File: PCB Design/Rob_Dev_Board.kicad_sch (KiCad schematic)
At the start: 0 parts

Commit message: Added component files for ESP32 and DRV8245H motor driver
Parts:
- added IC1: DRV8245HQPWPRQ1, SOP65P640X120-29N, symbol DRV8245H-Q1:DRV8245HQPWPRQ1
- added U1: ESP32-S3-WROOM-1U-N8R8, ESP32-S3-WROOM-1U-N8R8:XCVR_ESP32-S3-WROOM-1U-N8R8, symbol ESP32-S3-WROOM-1U-N8R8:ESP32-S3-WROOM-1U-N8R8
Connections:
- new net: U1.1 (GND), U1.40 (GND), U1.41_1 (GND), U1.41_2 (GND), U1.41_3 (GND), U1.41_4 (GND), U1.41_5 (GND), U1.41_6 (GND), U1.41_7 (GND), U1.41_8 (GND), U1.41_9 (GND)

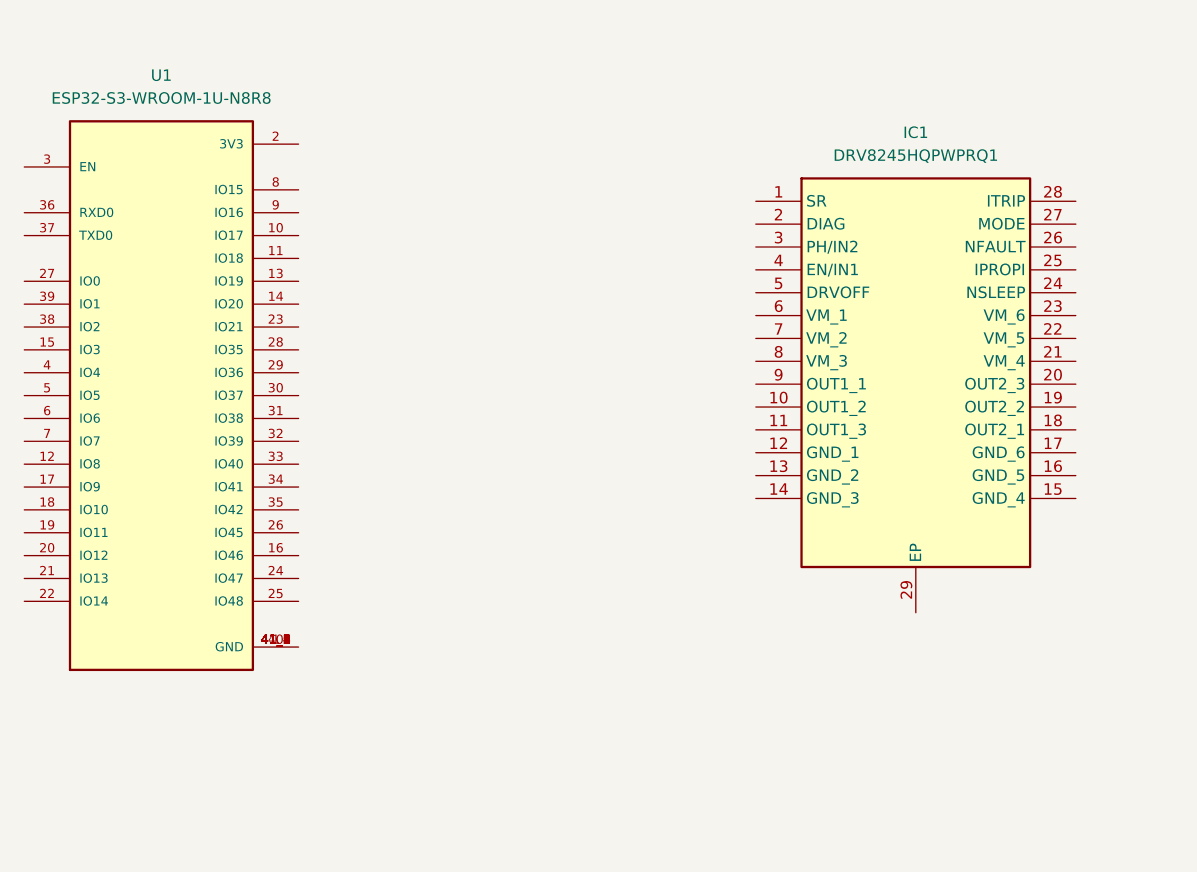
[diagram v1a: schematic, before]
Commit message: Changed components for ESP32 and motor driver to in stock options from supplier
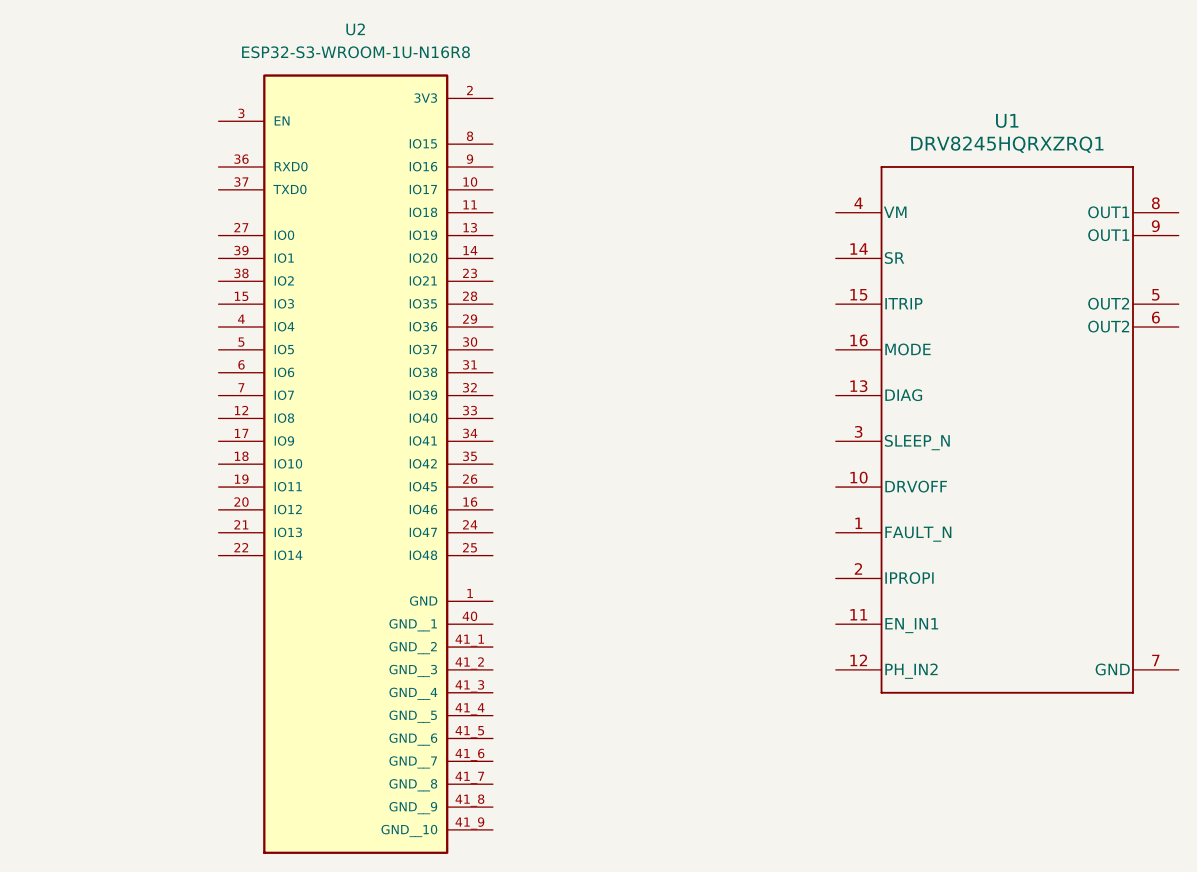
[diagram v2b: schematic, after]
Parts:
- removed IC1: DRV8245HQPWPRQ1, SOP65P640X120-29N, symbol DRV8245H-Q1:DRV8245HQPWPRQ1
- removed U1: ESP32-S3-WROOM-1U-N8R8, ESP32-S3-WROOM-1U-N8R8:XCVR_ESP32-S3-WROOM-1U-N8R8, symbol ESP32-S3-WROOM-1U-N8R8:ESP32-S3-WROOM-1U-N8R8
- added U1: DRV8245HQRXZRQ1, DRV8245H-Q1:RXZ0016A-MFG, symbol DRV8245H-Q1:DRV8245HQRXZRQ1
- added U2: ESP32-S3-WROOM-1U-N16R8, ESP32-S3-WROOM-N16R8:XCVR_ESP32-S3-WROOM-1U-N16R8, symbol ESP32-S3-WROOM-1U-N16R8:ESP32-S3-WROOM-1U-N16R8

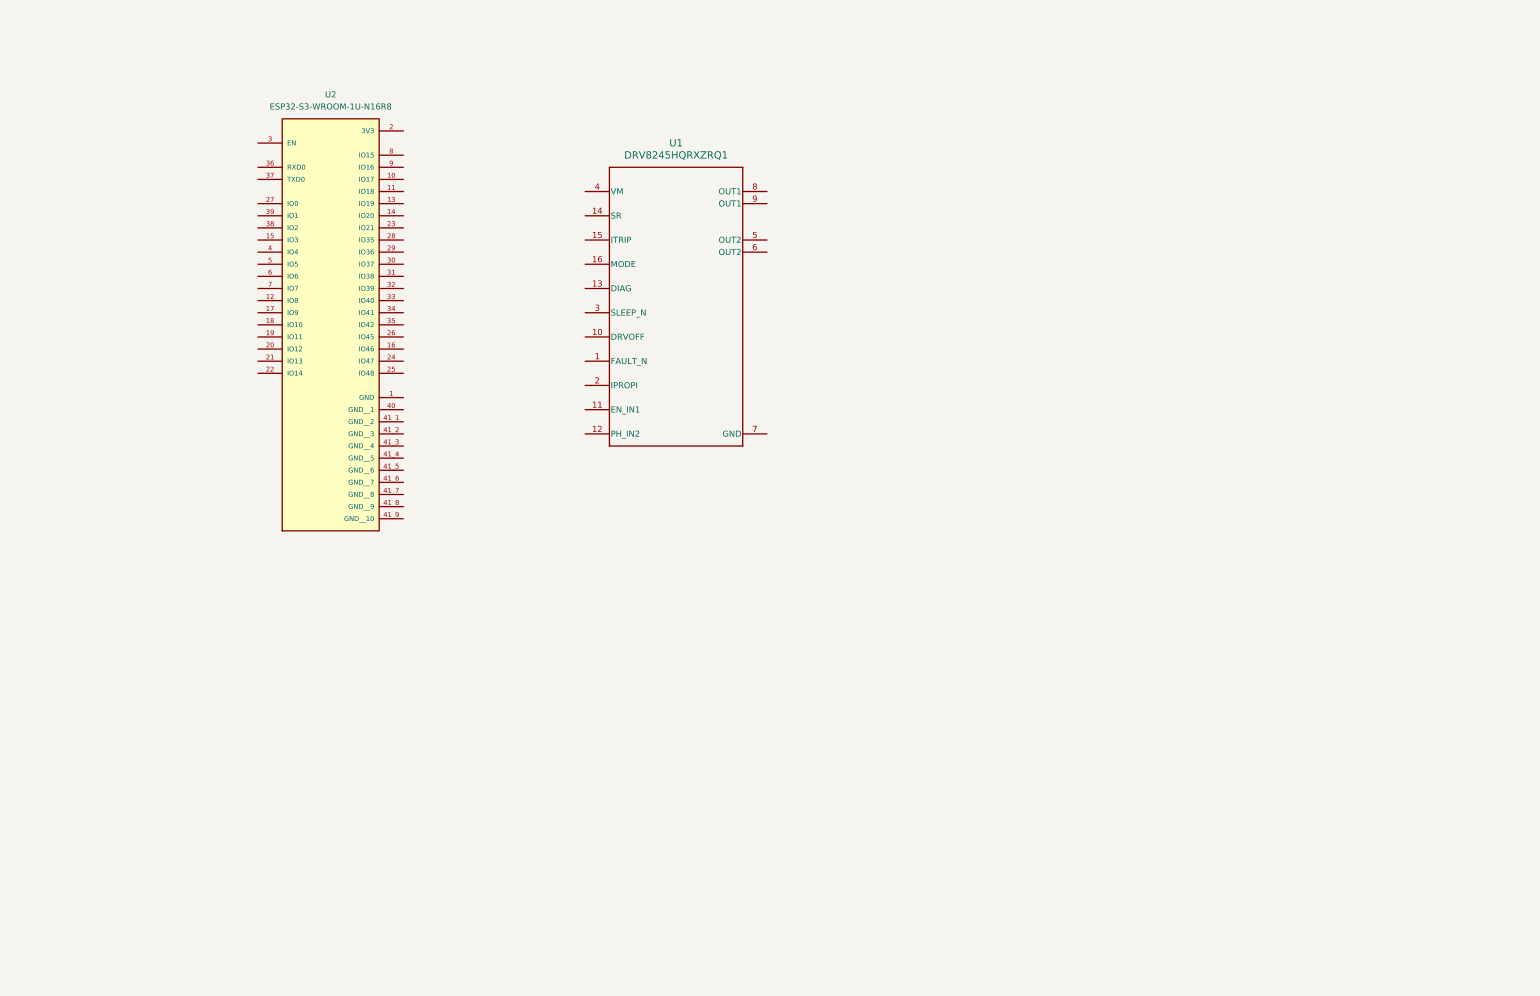
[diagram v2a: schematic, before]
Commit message: Added some more components to PCB design, added datasheet for possible BLDC motor driver
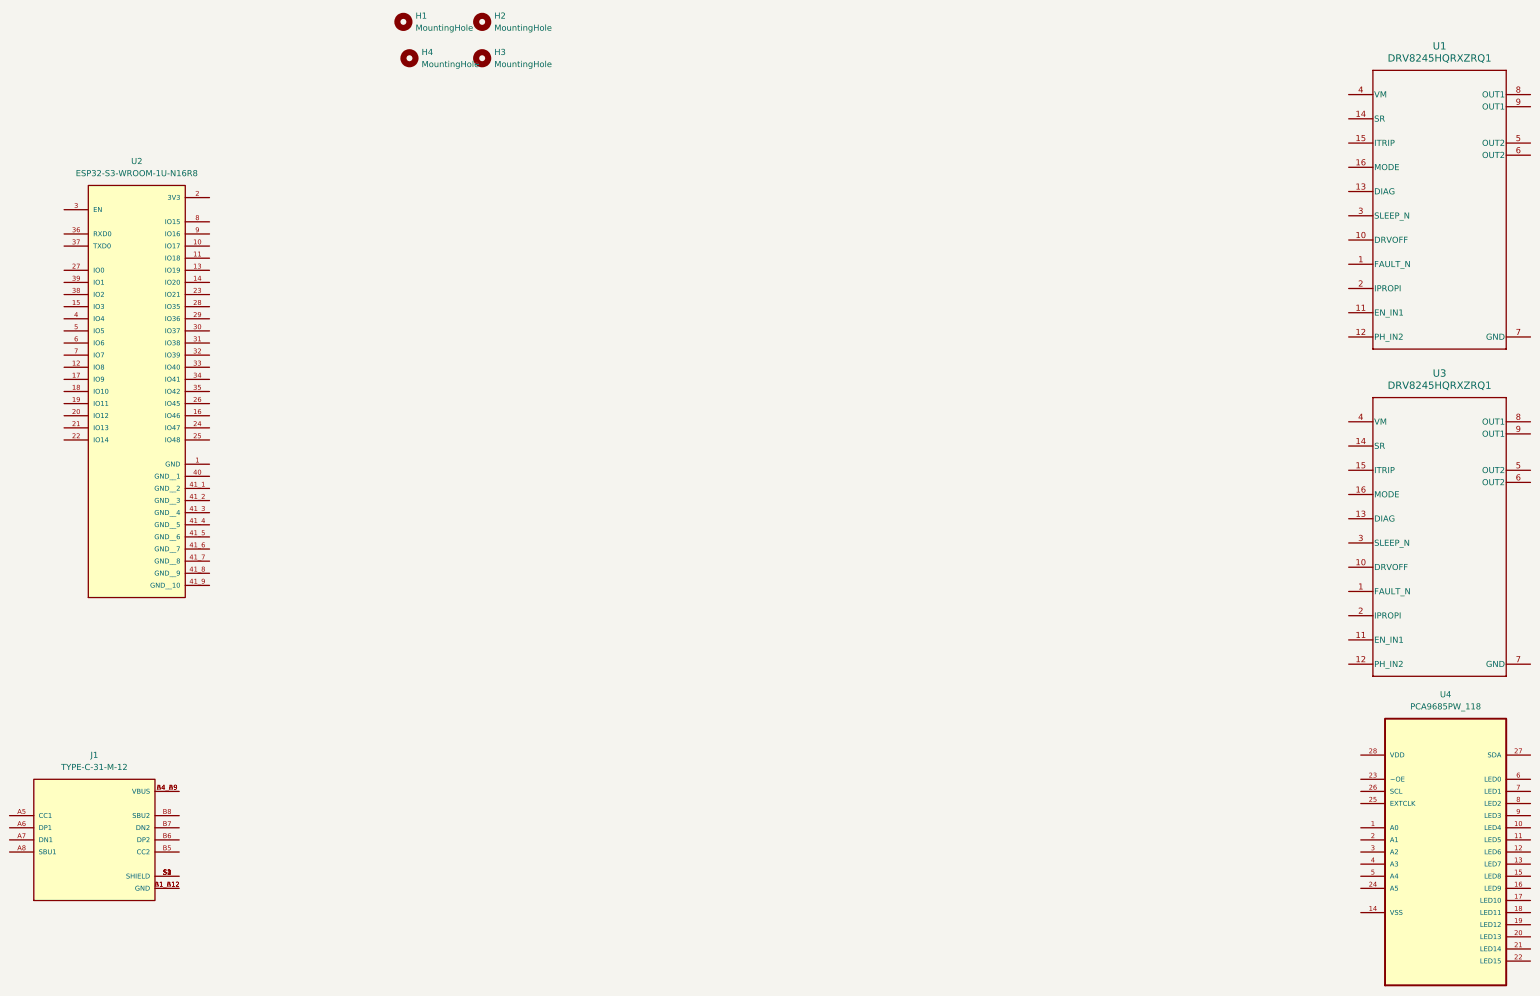
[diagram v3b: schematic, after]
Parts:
- added H1, H2, H3, H4: MountingHole, MountingHole:MountingHole_3.2mm_M3, symbol Mechanical:MountingHole
- added J1: TYPE-C-31-M-12, Type C Connector:HRO_TYPE-C-31-M-12, symbol Type C connector:TYPE-C-31-M-12
- added U3: DRV8245HQRXZRQ1, DRV8245H-Q1:RXZ0016A-MFG, symbol DRV8245H-Q1:DRV8245HQRXZRQ1
- added U4: PCA9685PW_118, PCA9685 PWM Servo Driver:SOP65P640X110-28N, symbol PCA9685 PWM Servo Driver:PCA9685PW_118
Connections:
- new net: J1.A1_B12 (GND), J1.B1_A12 (GND)
- new net: J1.A4_B9 (VBUS), J1.B4_A9 (VBUS)
- new net: J1.S1 (SHIELD), J1.S2 (SHIELD), J1.S3 (SHIELD), J1.S4 (SHIELD)
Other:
- moved on the sheet: U1, U2
